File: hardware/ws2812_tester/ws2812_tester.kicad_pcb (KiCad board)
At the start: 0 parts

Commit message: First draft component positioning
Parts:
- added C1: 1µF, Capacitor_SMD:C_0805_2012Metric_Pad1.18x1.45mm_HandSolder, F.Cu at (142.5, 112.5)
- added C2: 100nF, Capacitor_SMD:C_0805_2012Metric_Pad1.18x1.45mm_HandSolder, F.Cu at (144.5, 112.5)
- added F1: 1A, ws2812_tester:Belfuse_0ZCJ, F.Cu at (152.2, 115.5)
- added J1: USB_C_DEALON-USB-US31-106, ws2812_tester:DEALON_USB-US31-106, F.Cu at (150.5, 121.5)
- added J2: Pins_1-4, Connector_PinHeader_2.54mm:PinHeader_1x04_P2.54mm_Vertical, F.Cu at (161.5, 116.3)
- added J3: Conn_01x03, Connector_PinHeader_2.54mm:PinHeader_1x03_P2.54mm_Horizontal, F.Cu at (148.0, 104.2)
- added J4: Pins_5-8, Connector_PinHeader_2.54mm:PinHeader_1x04_P2.54mm_Vertical, F.Cu at (139.5, 116.3)
- added Q1: PMN48XP, Package_SO:TSOP-6_1.65x3.05mm_P0.95mm, F.Cu at (147.8, 115.5)
- added R1: 5.1kΩ, Resistor_SMD:R_0805_2012Metric_Pad1.20x1.40mm_HandSolder, F.Cu at (143.8, 120.0)
- added R2: 5.1kΩ, Resistor_SMD:R_0805_2012Metric_Pad1.20x1.40mm_HandSolder, F.Cu at (156.8, 120.0)
- added R3: 10kΩ, Resistor_SMD:R_0805_2012Metric_Pad1.20x1.40mm_HandSolder, F.Cu at (156.5, 113.5)
- added U1: ATtiny85-20S, Package_SO:SOIC-8W_5.3x5.3mm_P1.27mm, F.Cu at (150.2, 109.5)
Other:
- board outline added: 25 x 25 mm
- copper layers 0 -> 2

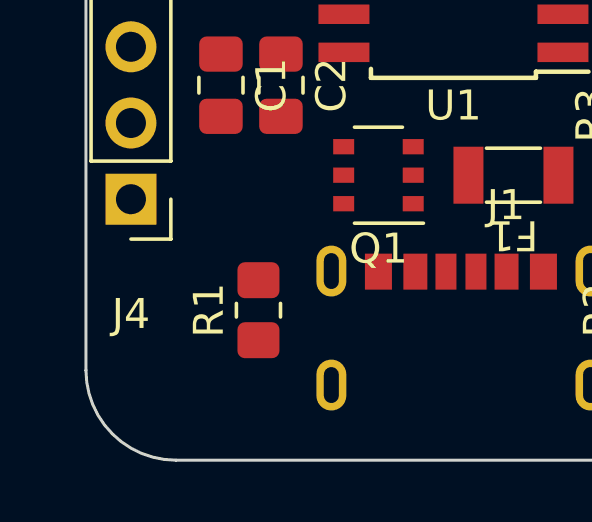
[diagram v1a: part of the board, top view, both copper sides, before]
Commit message: Adds power indication LEDs
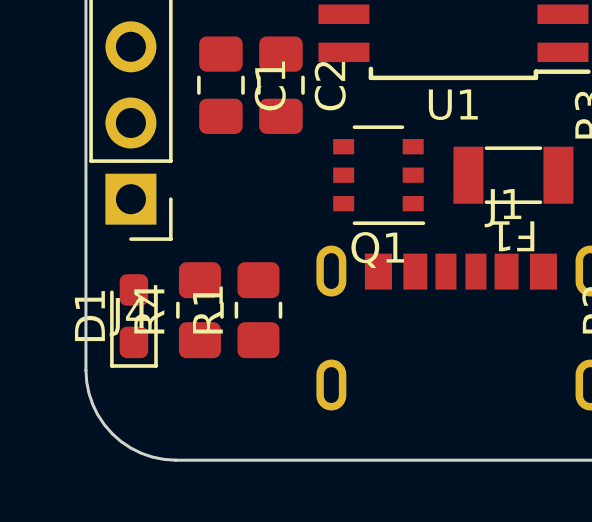
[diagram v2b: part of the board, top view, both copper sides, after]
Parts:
- added D1: LED, LED_SMD:LED_0603_1608Metric_Pad1.05x0.95mm_HandSolder, F.Cu at (139.6, 120.2)
- added R4: 1kΩ, Resistor_SMD:R_0805_2012Metric_Pad1.20x1.40mm_HandSolder, F.Cu at (141.8, 120.0)
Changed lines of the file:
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@@
   (net 11 "PB2")
   (net 12 "PB0")
+  (net 13 "Net-(D1-K)")
   (footprint "Connector_PinHeader_2.54mm:PinHeader_1x03_P2.54mm_Horizontal" (layer "F.Cu")
     (at 147.975 104.175 90)
@@
       (net 3 "+5V") (pinfunction "Pin_3") (pintype "passive"))
     (model "${KICAD6_3DMODEL_DIR}/Connector_PinHeader_2.54mm.3dshapes/PinHeader_1x03_P2.54mm_Horizontal.wrl"
+      (offset (xyz 0 0 0))
+      (scale (xyz 1 1 1))
+      (rotate (xyz 0 0 0))
+    )
+  )
+  (footprint "LED_SMD:LED_0603_1608Metric_Pad1.05x0.95mm_HandSolder" (layer "F.Cu")
+    (at 139.6 120.2 90)
+    (descr "LED SMD 0603 (1608 Metric), square (rectangular) end terminal, IPC_7351 nominal, (Body size source: http://www.tortai-tech.com/upload/download/2011102023233369053.pdf), generated with kicad-footprint-generator")
+    (tags "LED handsolder")
+    (property "Sheetfile" "ws2812_tester.kicad_sch")
+    (property "Sheetname" "")
+    (property "ki_description" "Light emitting diode")
+    (property "ki_keywords" "LED diode")
+    (attr smd)
+    (fp_text reference "D1" (at 0 -1.43 90) (layer "F.SilkS")
+        (effects (font (size 1 1) (thickness 0.15)))
+    )
+    (fp_text value "LED" (at 0 1.43 90) (layer "F.Fab")
+        (effects (font (size 1 1) (thickness 0.15)))
+    )
+    (fp_text user "${REFERENCE}" (at 0 0 90) (layer "F.Fab")
+        (effects (font (size 0.4 0.4) (thickness 0.06)))
+    )
+    (fp_line (start -1.66 -0.735) (end -1.66 0.735)
+      (stroke (width 0.12) (type solid)) (layer "F.SilkS"))
+    (fp_line (start -1.66 0.735) (end 0.8 0.735)
+      (stroke (width 0.12) (type solid)) (layer "F.SilkS"))
+    (fp_line (start 0.8 -0.735) (end -1.66 -0.735)
+      (stroke (width 0.12) (type solid)) (layer "F.SilkS"))
+    (fp_line (start -1.65 -0.73) (end 1.65 -0.73)
+      (stroke (width 0.05) (type solid)) (layer "F.CrtYd"))
+    (fp_line (start -1.65 0.73) (end -1.65 -0.73)
+      (stroke (width 0.05) (type solid)) (layer "F.CrtYd"))
+    (fp_line (start 1.65 -0.73) (end 1.65 0.73)
+      (stroke (width 0.05) (type solid)) (layer "F.CrtYd"))
+    (fp_line (start 1.65 0.73) (end -1.65 0.73)
+      (stroke (width 0.05) (type solid)) (layer "F.CrtYd"))
+    (fp_line (start -0.8 -0.1) (end -0.8 0.4)
+      (stroke (width 0.1) (type solid)) (layer "F.Fab"))
+    (fp_line (start -0.8 0.4) (end 0.8 0.4)
+      (stroke (width 0.1) (type solid)) (layer "F.Fab"))
+    (fp_line (start -0.5 -0.4) (end -0.8 -0.1)
+      (stroke (width 0.1) (type solid)) (layer "F.Fab"))
+    (fp_line (start 0.8 -0.4) (end -0.5 -0.4)
+      (stroke (width 0.1) (type solid)) (layer "F.Fab"))
+    (fp_line (start 0.8 0.4) (end 0.8 -0.4)
+      (stroke (width 0.1) (type solid)) (layer "F.Fab"))
+    (pad "1" smd roundrect (at -0.875 0 90) (size 1.05 0.95) (layers "F.Cu" "F.Paste" "F.Mask") (roundrect_rratio 0.25)
+      (net 13 "Net-(D1-K)") (pinfunction "K") (pintype "passive"))
+    (pad "2" smd roundrect (at 0.875 0 90) (size 1.05 0.95) (layers "F.Cu" "F.Paste" "F.Mask") (roundrect_rratio 0.25)
+      (net 1 "VCC") (pinfunction "A") (pintype "passive"))
+    (model "${KICAD6_3DMODEL_DIR}/LED_SMD.3dshapes/LED_0603_1608Metric.wrl"
       (offset (xyz 0 0 0))
       (scale (xyz 1 1 1))
@@
       (net 4 "Net-(Q1-D)") (pintype "passive"))
   )
+  (footprint "Resistor_SMD:R_0805_2012Metric_Pad1.20x1.40mm_HandSolder" (layer "F.Cu")
+    (at 141.8 120 90)
+    (descr "Resistor SMD 0805 (2012 Metric), square (rectangular) end terminal, IPC_7351 nominal with elongated pad for handsoldering. (Body size source: IPC-SM-782 page 72, https://www.pcb-3d.com/wordpress/wp-content/uploads/ipc-sm-782a_amendment_1_and_2.pdf), generated with kicad-footprint-generator")
+    (tags "resistor handsolder")
+    (property "Sheetfile" "ws2812_tester.kicad_sch")
+    (property "Sheetname" "")
+    (property "ki_description" "Resistor, small US symbol")
+    (property "ki_keywords" "r resistor")
+    (attr smd)
+    (fp_text reference "R4" (at 0 -1.65 90) (layer "F.SilkS")
+        (effects (font (size 1 1) (thickness 0.15)))
+    )
+    (fp_text value "1kΩ" (at 0 1.65 90) (layer "F.Fab")
+        (effects (font (size 1 1) (thickness 0.15)))
+    )
+    (fp_text user "${REFERENCE}" (at 0 0 90) (layer "F.Fab")
+        (effects (font (size 0.5 0.5) (thickness 0.08)))
+    )
+    (fp_line (start -0.227064 -0.735) (end 0.227064 -0.735)
+      (stroke (width 0.12) (type solid)) (layer "F.SilkS"))
+    (fp_line (start -0.227064 0.735) (end 0.227064 0.735)
+      (stroke (width 0.12) (type solid)) (layer "F.SilkS"))
+    (fp_line (start -1.85 -0.95) (end 1.85 -0.95)
+      (stroke (width 0.05) (type solid)) (layer "F.CrtYd"))
+    (fp_line (start -1.85 0.95) (end -1.85 -0.95)
+      (stroke (width 0.05) (type solid)) (layer "F.CrtYd"))
+    (fp_line (start 1.85 -0.95) (end 1.85 0.95)
+      (stroke (width 0.05) (type solid)) (layer "F.CrtYd"))
+    (fp_line (start 1.85 0.95) (end -1.85 0.95)
+      (stroke (width 0.05) (type solid)) (layer "F.CrtYd"))
+    (fp_line (start -1 -0.625) (end 1 -0.625)
+      (stroke (width 0.1) (type solid)) (layer "F.Fab"))
+    (fp_line (start -1 0.625) (end -1 -0.625)
+      (stroke (width 0.1) (type solid)) (layer "F.Fab"))
+    (fp_line (start 1 -0.625) (end 1 0.625)
+      (stroke (width 0.1) (type solid)) (layer "F.Fab"))
+    (fp_line (start 1 0.625) (end -1 0.625)
+      (stroke (width 0.1) (type solid)) (layer "F.Fab"))
+    (pad "1" smd roundrect (at -1 0 90) (size 1.2 1.4) (layers "F.Cu" "F.Paste" "F.Mask") (roundrect_rratio 0.208333)
+      (net 13 "Net-(D1-K)") (pintype "passive"))
+    (pad "2" smd roundrect (at 1 0 90) (size 1.2 1.4) (layers "F.Cu" "F.Paste" "F.Mask") (roundrect_rratio 0.208333)
+      (net 2 "GND") (pintype "passive"))
+    (model "${KICAD6_3DMODEL_DIR}/Resistor_SMD.3dshapes/R_0805_2012Metric.wrl"
+      (offset (xyz 0 0 0))
+      (scale (xyz 1 1 1))
+      (rotate (xyz 0 0 0))
+    )
+  )
   (footprint "Package_SO:TSOP-6_1.65x3.05mm_P0.95mm" (layer "F.Cu")

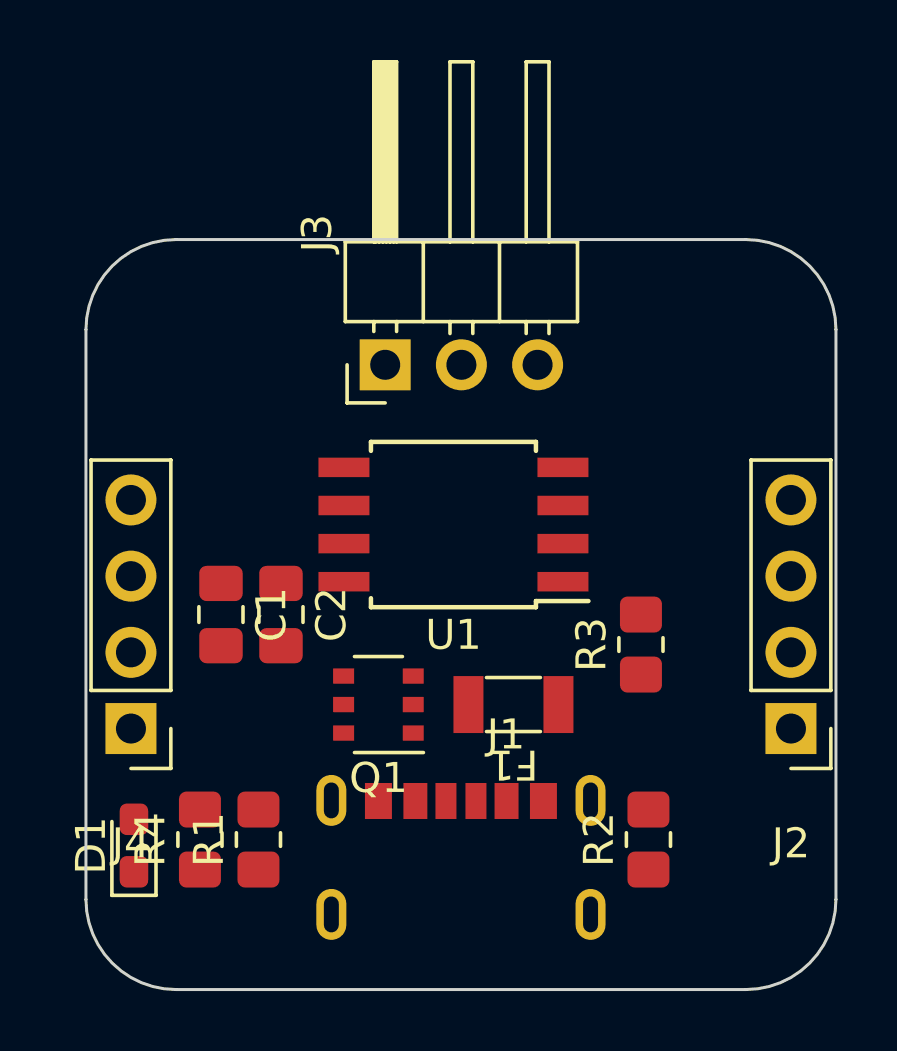
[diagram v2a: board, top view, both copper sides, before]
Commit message: Adjusts component alignment
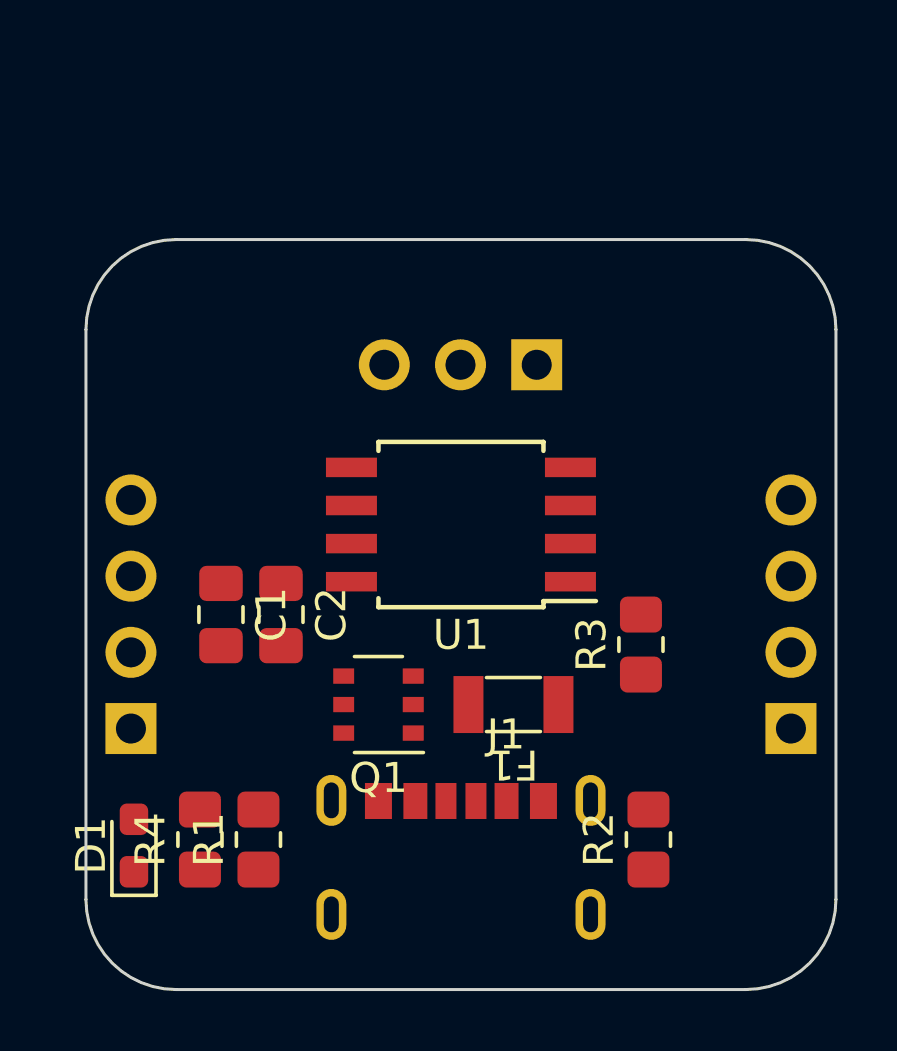
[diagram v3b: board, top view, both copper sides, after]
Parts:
- J2, J3, J4: moved to B.Cu
- moved J3 5.05 mm to (153.0, 104.2)
- moved U1 0.25 mm to (150.5, 109.5)
- turned J2 to 0 degrees
- turned J4 to 0 degrees

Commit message: Draft routing for all tracks
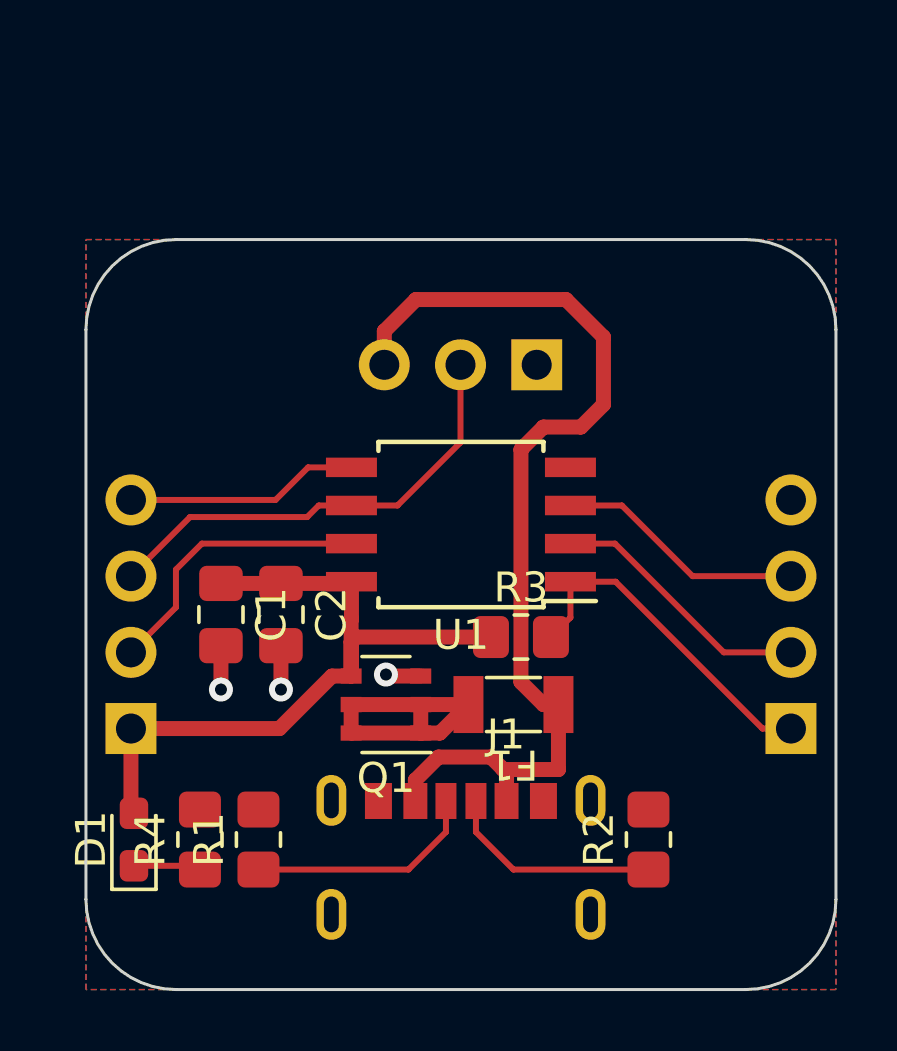
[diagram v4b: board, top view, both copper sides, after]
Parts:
- moved R3 4.01 mm to (152.5, 113.2), turned to 0 degrees
- moved Q1 0.25 mm to (148.0, 115.5)
- moved D1 0.20 mm to (139.6, 120.0)
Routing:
- net +5V: track 0.00 -> 33.6 mm
- net VCC: track 0.00 -> 24.3 mm
- net PB1/LED_DATA: track 0.00 -> 15.4 mm
- net PB5/RST: track 0.00 -> 11.5 mm
- net Net-(Q1-D): track 0.00 -> 10.1 mm
- net PB2: track 0.00 -> 9.59 mm
- net PB3: track 0.00 -> 8.85 mm
- net PB4: track 0.00 -> 8.33 mm
- net Net-(J1-CC1): track 0.00 -> 7.80 mm
- net PB0: track 0.00 -> 7.80 mm
- net Net-(J1-CC2): track 0.00 -> 7.30 mm
- net GND: track 0.00 -> 4.11 mm, vias 0 -> 3
- net Net-(D1-K): track 0.00 -> 2.25 mm
- added copper zone on B.Cu, net GND
- added copper zone on F.Cu, net GND

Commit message: Fixes some DRC errors
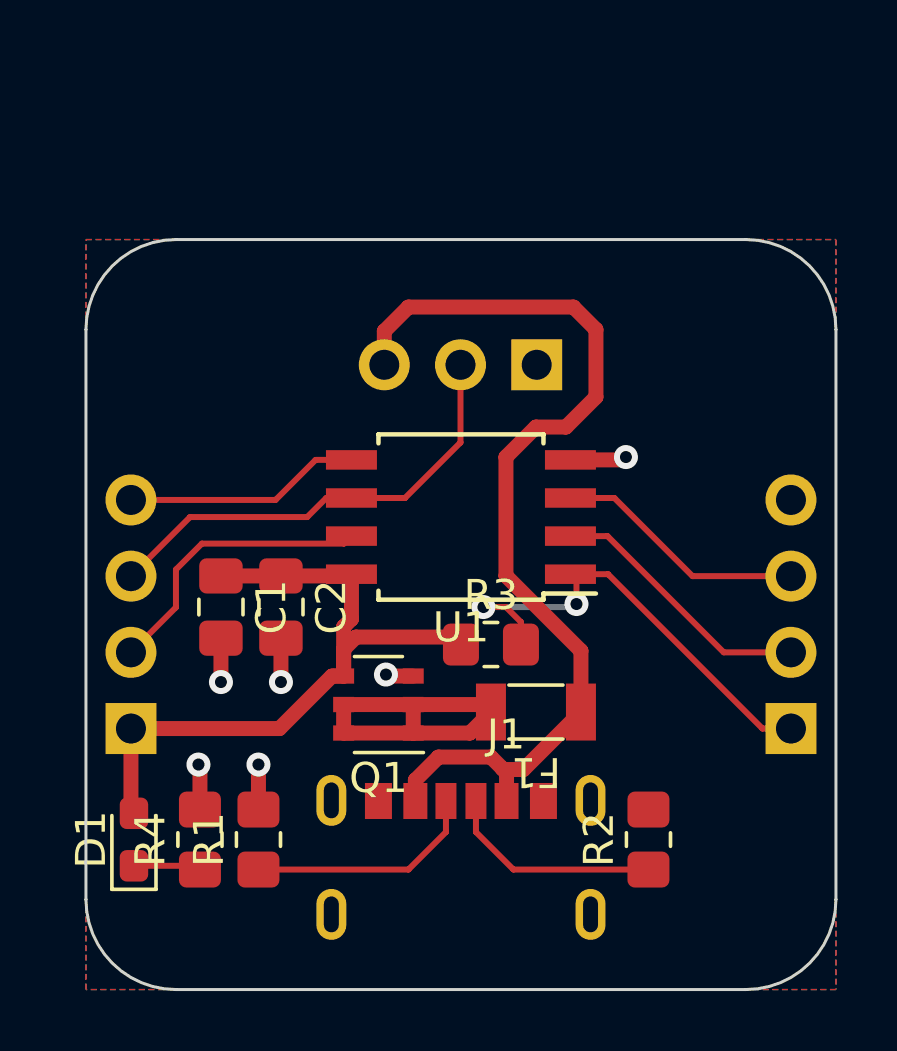
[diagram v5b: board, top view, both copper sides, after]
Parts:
- moved R3 1.03 mm to (151.5, 113.5)
- moved F1 0.79 mm to (153.0, 115.8)
- moved C1 0.25 mm to (142.5, 112.2)
- moved C2 0.25 mm to (144.5, 112.2)
- moved Q1 0.25 mm to (147.8, 115.5)
- moved U1 0.25 mm to (150.5, 109.2)
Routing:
- net GND: track 4.11 -> 8.77 mm, vias 3 -> 6
- net PB5/RST: track 11.5 -> 15.9 mm, vias 0 -> 2
- net Net-(Q1-D): track 10.1 -> 12.1 mm
- net VCC: track 24.3 -> 23.6 mm
- net +5V: track 33.6 -> 33.1 mm

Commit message: Routes 5v from LED strip on the bottom layer
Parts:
- moved R3 1.65 mm to (153.2, 113.5)
- moved Q1 0.25 mm to (148.0, 115.5)
- moved F1 0.15 mm to (153.2, 115.8)
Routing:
- net +5V: track 33.1 -> 28.6 mm, vias 0 -> 1
- net PB5/RST: track 15.9 -> 11.8 mm, vias 2 -> 0
- net VCC: track 23.6 -> 24.4 mm

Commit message: Updates PCB with new schematics
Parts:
- removed Q1: PMN48XP, Package_SO:TSOP-6_1.65x3.05mm_P0.95mm
- added D2: MBR120, Diode_SMD:D_SOD-123, F.Cu at (144.2, 104.2)
- moved F1 4.65 mm to (148.5, 115.8)
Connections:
- F1 pad 1: +5V -> Net-(J1-VBUS)
- F1 pad 2: Net-(Q1-D) -> VCC
- J1 pad A9: +5V -> Net-(J1-VBUS)
- J1 pad B9: +5V -> Net-(J1-VBUS)
- J3 pad 3: +5V -> 5V_out
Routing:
- net +5V: track 28.6 -> 0.00 mm, vias 1 -> 0
- net VCC: track 24.4 -> 39.6 mm, vias 0 -> 1
- net Net-(Q1-D): track 11.9 -> 0.00 mm
- net Net-(J1-VBUS): track 0.00 -> 6.82 mm
- net 5V_out: track 0.00 -> 2.08 mm
- net GND: track 8.27 -> 7.08 mm, vias 6 -> 5
